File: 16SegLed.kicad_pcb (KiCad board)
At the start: 2 copper layers, 99.9 x 79.6 mm, 57 parts, among them J1 Conn_01x10, J2 Conn_01x10, J3 Conn_01x10, J4 Conn_01x06_Socket, J5 Conn_01x04_Pin, J6 Conn_01x04_Pin, Q1 BSS138, Q2 BSS138, SW1 SW_Push, SW2 SW_Push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

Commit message: Use meaningful segment net names
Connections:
- net /DisplayGroup0/SEG0 renamed /DisplayGroup0/SEG_{E}
- net /DisplayGroup0/SEG1 renamed /DisplayGroup0/SEG_{N}
- net /DisplayGroup0/SEG10 renamed /DisplayGroup0/SEG_{G1}
- net /DisplayGroup0/SEG11 renamed /DisplayGroup0/SEG_{K}
- net /DisplayGroup0/SEG12 renamed /DisplayGroup0/SEG_{J}
- net /DisplayGroup0/SEG13 renamed /DisplayGroup0/SEG_{H}
- net /DisplayGroup0/SEG14 renamed /DisplayGroup0/SEG_{F}
- net /DisplayGroup0/SEG2 renamed /DisplayGroup0/SEG_{M}
- net /DisplayGroup0/SEG3 renamed /DisplayGroup0/SEG_{L}
- net /DisplayGroup0/SEG4 renamed /DisplayGroup0/SEG_{G2}
- net /DisplayGroup0/SEG5 renamed /DisplayGroup0/SEG_{D}
- net /DisplayGroup0/SEG6 renamed /DisplayGroup0/SEG_{dp}
- net /DisplayGroup0/SEG7 renamed /DisplayGroup0/SEG_{C}
- net /DisplayGroup0/SEG8 renamed /DisplayGroup0/SEG_{B}
- net /DisplayGroup0/SEG9 renamed /DisplayGroup0/SEG_{A}
- net /DisplayGroup1/SEG0 renamed /DisplayGroup1/SEG_{E}
- net /DisplayGroup1/SEG1 renamed /DisplayGroup1/SEG_{N}
- net /DisplayGroup1/SEG10 renamed /DisplayGroup1/SEG_{G1}
- net /DisplayGroup1/SEG11 renamed /DisplayGroup1/SEG_{K}
- net /DisplayGroup1/SEG12 renamed /DisplayGroup1/SEG_{J}
- net /DisplayGroup1/SEG13 renamed /DisplayGroup1/SEG_{H}
- net /DisplayGroup1/SEG14 renamed /DisplayGroup1/SEG_{F}
- net /DisplayGroup1/SEG2 renamed /DisplayGroup1/SEG_{M}
- net /DisplayGroup1/SEG3 renamed /DisplayGroup1/SEG_{L}
- net /DisplayGroup1/SEG4 renamed /DisplayGroup1/SEG_{G2}
- net /DisplayGroup1/SEG5 renamed /DisplayGroup1/SEG_{D}
- net /DisplayGroup1/SEG6 renamed /DisplayGroup1/SEG_{dp}
- net /DisplayGroup1/SEG7 renamed /DisplayGroup1/SEG_{C}
- net /DisplayGroup1/SEG8 renamed /DisplayGroup1/SEG_{B}
- net /DisplayGroup1/SEG9 renamed /DisplayGroup1/SEG_{A}

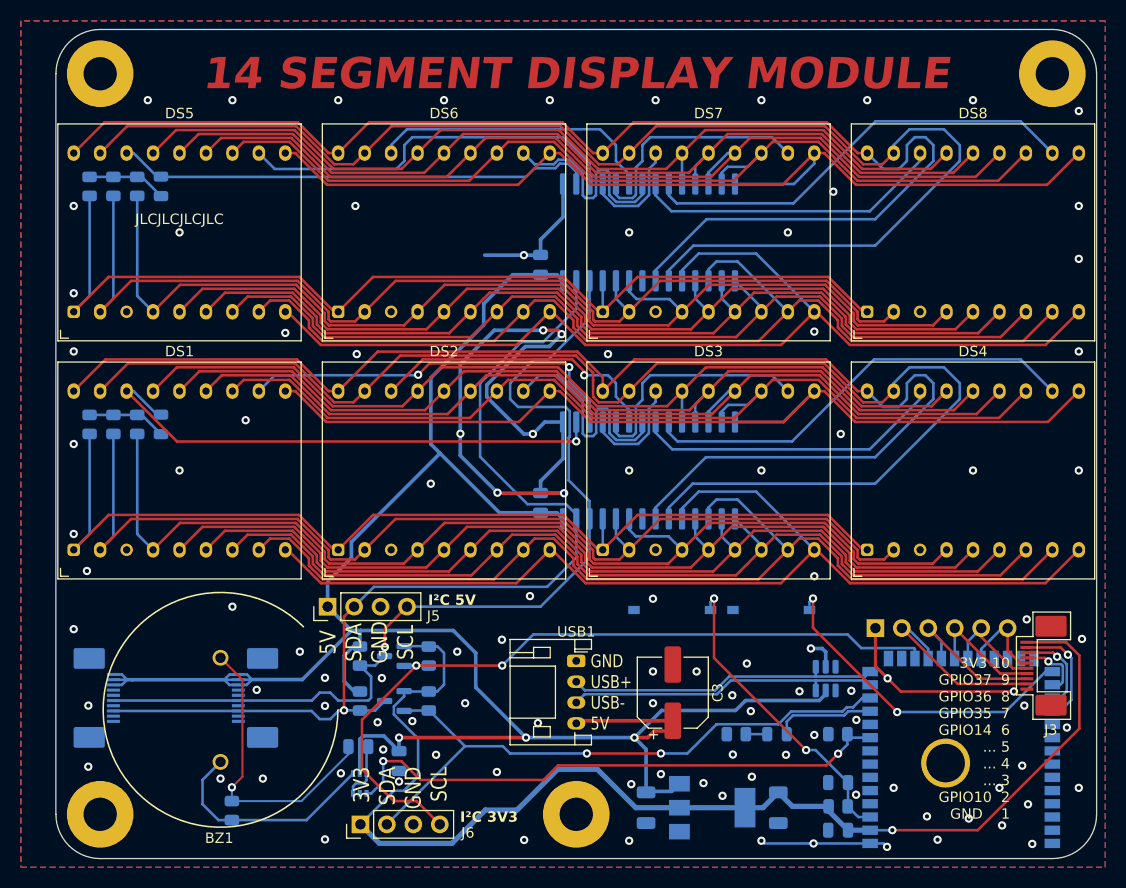
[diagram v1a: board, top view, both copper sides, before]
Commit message: Rearrange ROW assignment so digits are scanned consecutively from left to right
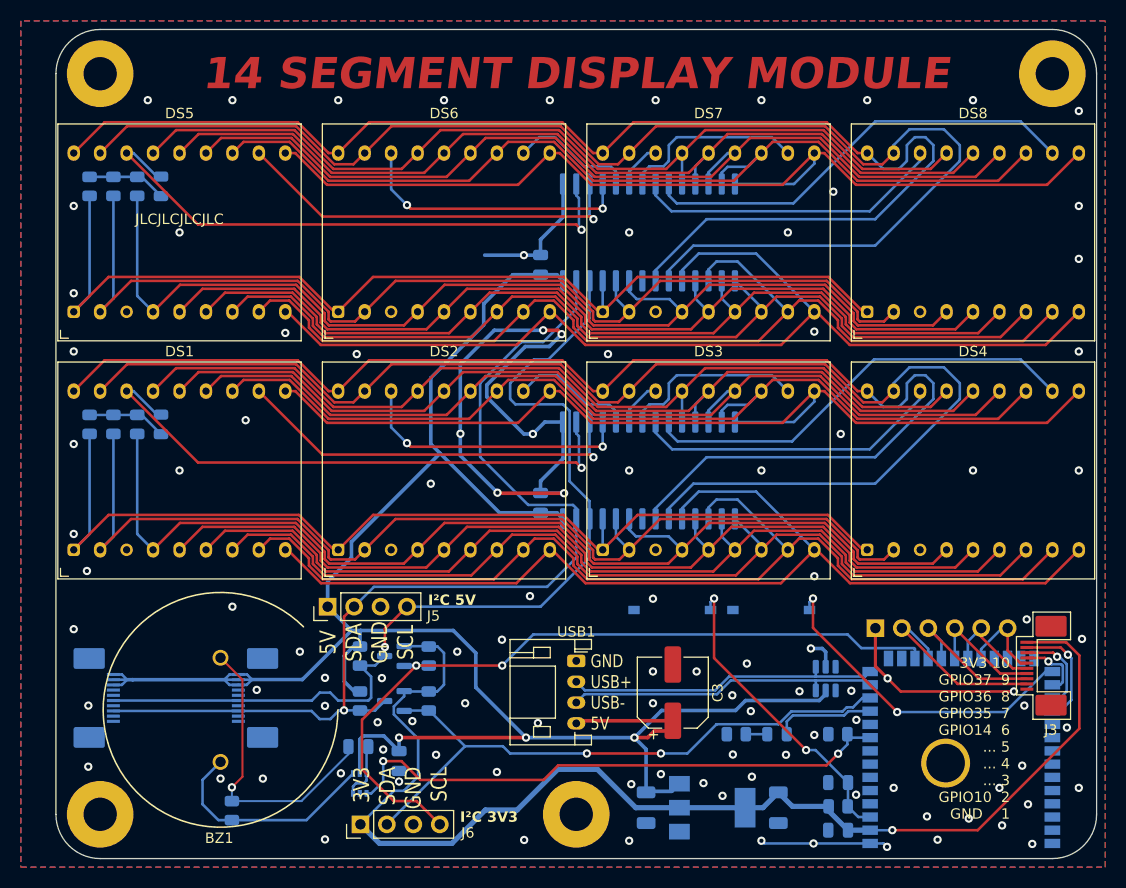
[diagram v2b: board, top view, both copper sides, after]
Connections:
- DS2 pad 11: /DisplayGroup0/COM5 -> /DisplayGroup0/COM3
- DS2 pad 16: /DisplayGroup0/COM4 -> /DisplayGroup0/COM2
- DS3 pad 11: /DisplayGroup0/COM3 -> /DisplayGroup0/COM5
- DS3 pad 16: /DisplayGroup0/COM2 -> /DisplayGroup0/COM4
- DS6 pad 11: /DisplayGroup1/COM5 -> /DisplayGroup1/COM3
- DS6 pad 16: /DisplayGroup1/COM4 -> /DisplayGroup1/COM2
- DS7 pad 11: /DisplayGroup1/COM3 -> /DisplayGroup1/COM5
- DS7 pad 16: /DisplayGroup1/COM2 -> /DisplayGroup1/COM4
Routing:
- net /DisplayGroup0/COM4: track 28.3 -> 4.47 mm, vias 1 -> 0
- net /DisplayGroup1/COM4: track 27.9 -> 4.47 mm
- net /DisplayGroup0/COM2: track 10.6 -> 26.9 mm, vias 0 -> 2
- net /DisplayGroup1/COM2: track 10.6 -> 26.9 mm, vias 0 -> 2
- net /DisplayGroup0/COM3: track 23.2 -> 12.0 mm
- net /DisplayGroup1/COM3: track 23.2 -> 12.1 mm
- net /DisplayGroup1/COM0: track 46.1 -> 55.6 mm, vias 0 -> 1
- net /DisplayGroup0/COM5: track 22.5 -> 18.0 mm
- net /DisplayGroup0/COM0: track 51.3 -> 55.6 mm
- net /DisplayGroup1/COM5: track 21.0 -> 18.0 mm
- net /DisplayGroup0/SEG_{H}: track 130.7 -> 128.5 mm
- net /DisplayGroup0/SEG_{F}: track 128.2 -> 126.6 mm
- net /DisplayGroup0/COM1: track 37.1 -> 38.3 mm, vias 2 -> 1
- net /DisplayGroup0/SEG_{B}: track 92.4 -> 93.2 mm
- net /DisplayGroup1/COM1: track 37.5 -> 38.3 mm, vias 0 -> 1
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
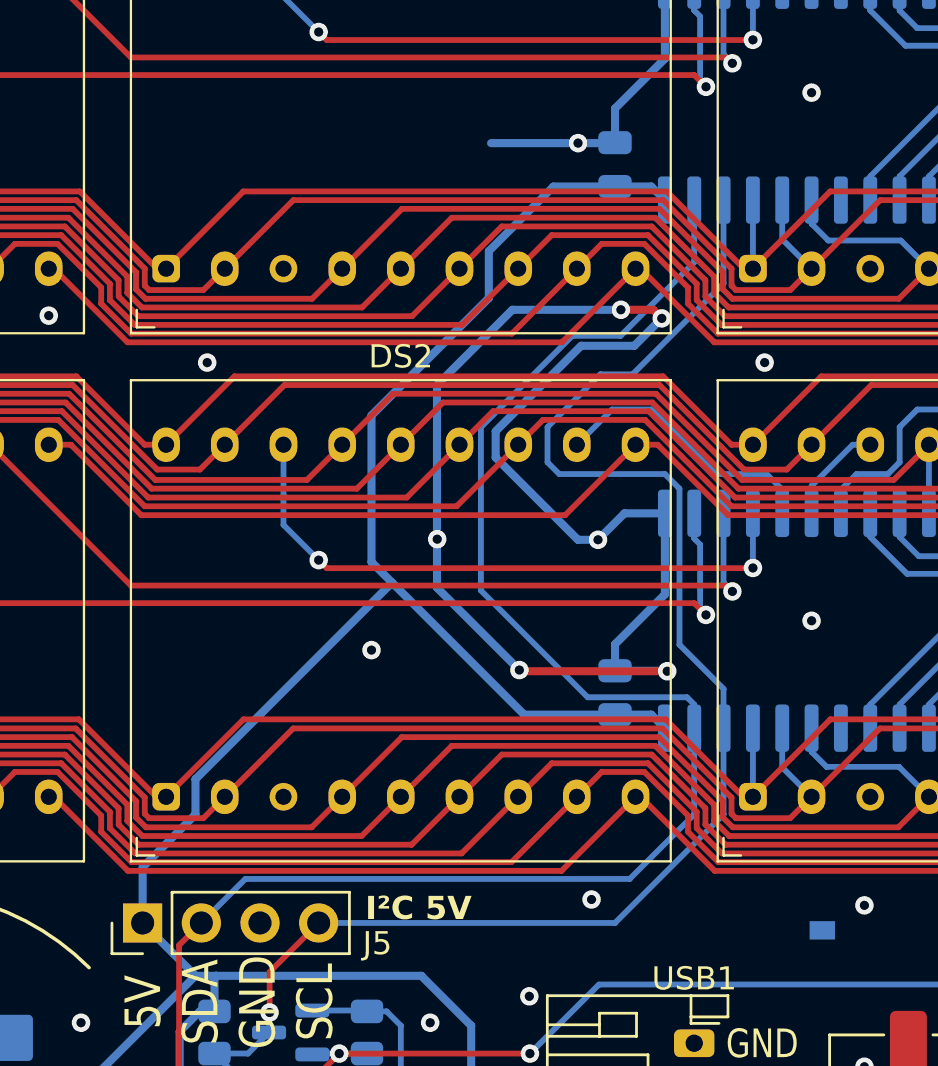
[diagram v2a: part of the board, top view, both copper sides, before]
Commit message: Improve routing of power and I2C nets for LED drivers
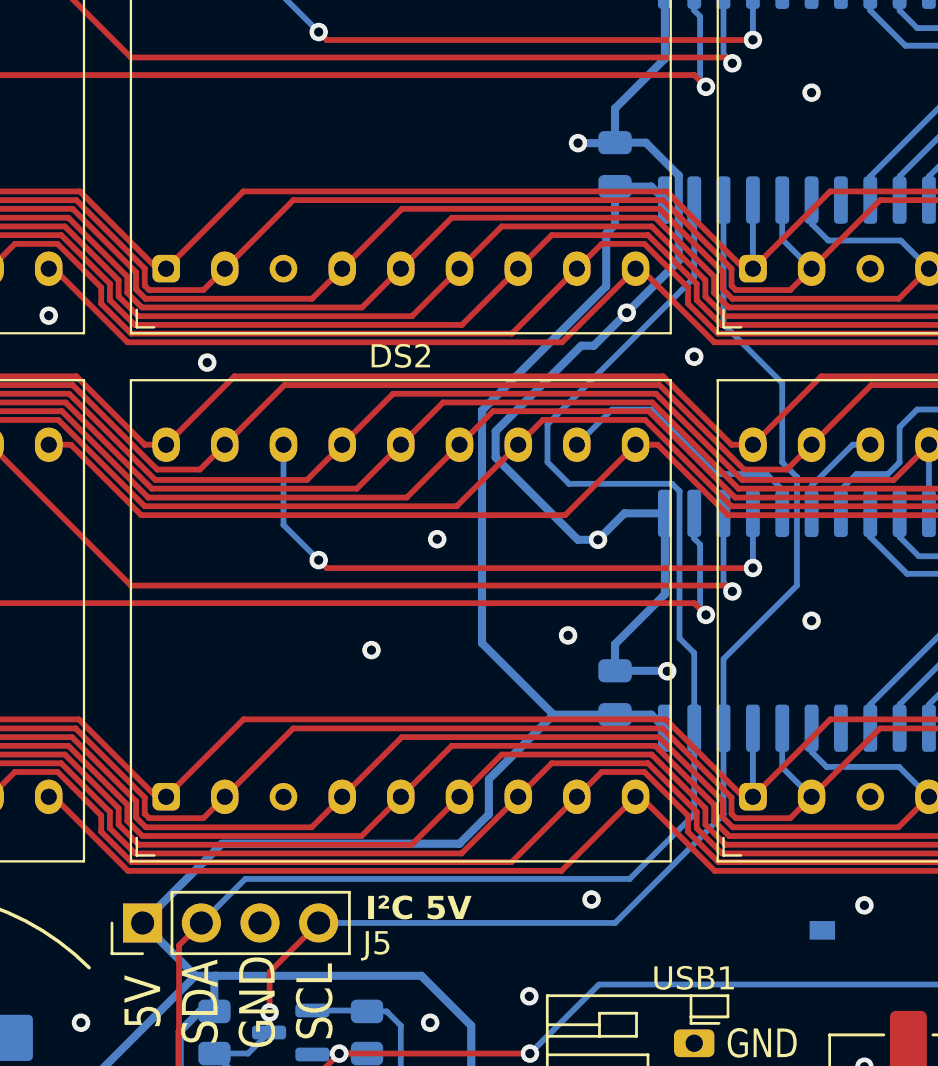
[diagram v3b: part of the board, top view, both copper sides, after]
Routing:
- net GND: track 107.6 -> 81.2 mm, vias 108 -> 107
- net /SCL5V: track 93.3 -> 86.1 mm
- net /SDA5V: track 98.7 -> 95.2 mm
- net +5V: track 203.1 -> 200.0 mm
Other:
- board text added: "2024-JAN-07"
- board text removed: "2024-JAN-06"

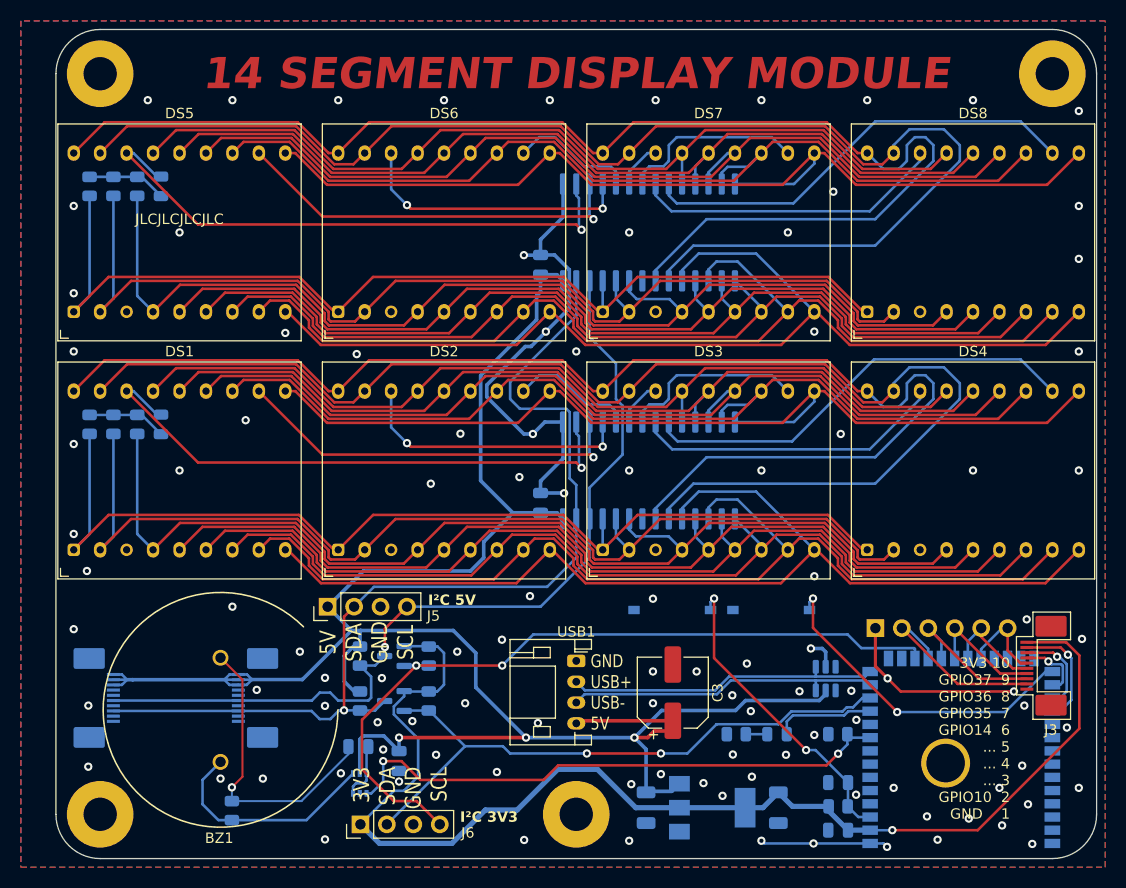
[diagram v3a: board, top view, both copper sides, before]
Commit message: Rearrange GND vias
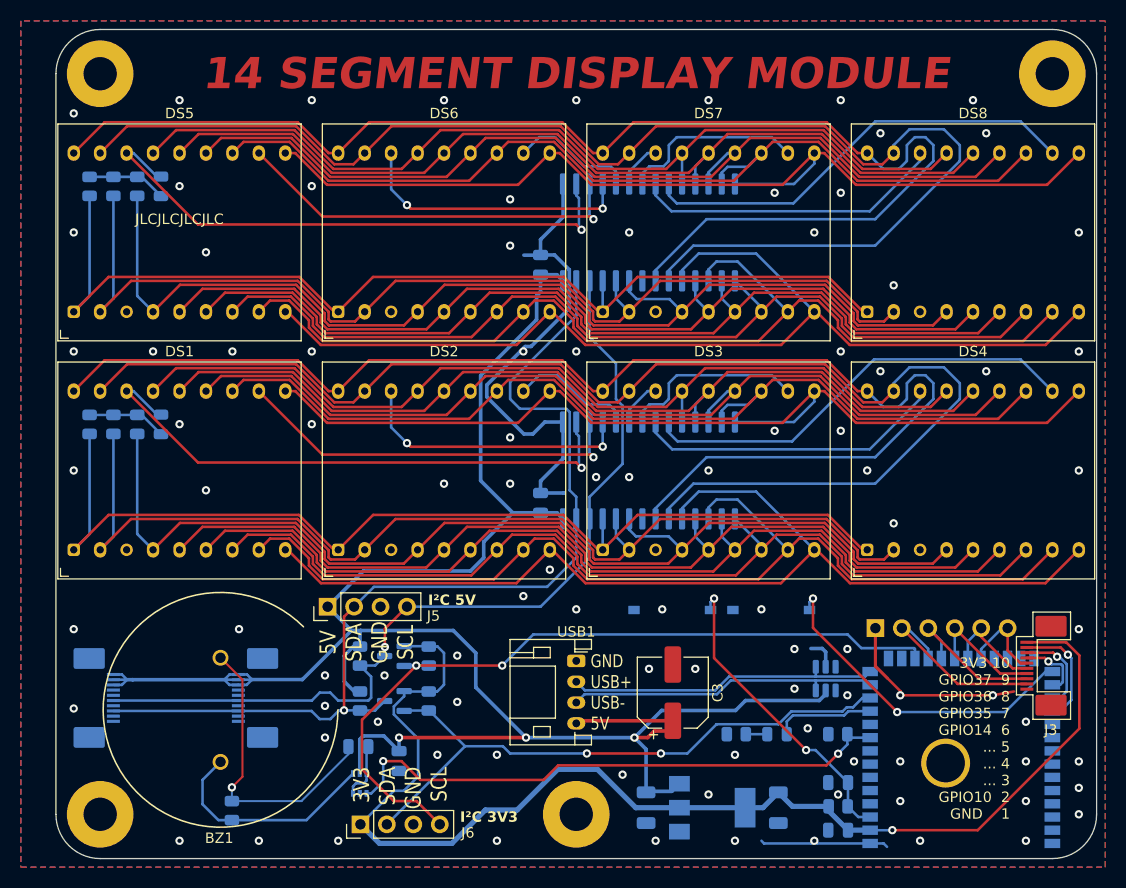
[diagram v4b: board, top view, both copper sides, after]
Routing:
- net GND: track 81.2 -> 81.8 mm, vias 107 -> 96

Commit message: Connect mounting holes to ground
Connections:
- H1 pad 1: (no net) -> GND
- H2 pad 1: (no net) -> GND
- H3 pad 1: (no net) -> GND
- H4 pad 1: (no net) -> GND
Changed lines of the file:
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@@
     (property "Sheetfile" "16SegLed.kicad_sch")
     (property "Sheetname" "")
-    (property "dnp" "")
-    (property "exclude_from_bom" "")
-    (property "ki_description" "Mounting Hole without connection")
+    (property "ki_description" "Mounting Hole with connection")
     (property "ki_keywords" "mounting hole")
-    (attr exclude_from_pos_files exclude_from_bom)
+    (attr exclude_from_pos_files)
     (fp_text reference "H2" (at 0 -4.2) (layer "F.SilkS") hide
         (effects (font (size 1 1) (thickness 0.15)))
@@
         (effects (font (size 1 1) (thickness 0.15)))
     )
+    (fp_text user "${REFERENCE}" (at 0 0) (layer "F.Fab")
+        (effects (font (size 1 1) (thickness 0.15)))
+    )
     (fp_circle (center 0 0) (end 3.2 0)
       (stroke (width 0.15) (type solid)) (fill none) (layer "Cmts.User"))
     (fp_circle (center 0 0) (end 3.45 0)
       (stroke (width 0.05) (type solid)) (fill none) (layer "F.CrtYd"))
-    (pad "1" thru_hole circle (at 0 0) (size 6.4 6.4) (drill 3.2) (layers "*.Cu" "*.Mask"))
+    (pad "1" thru_hole circle (at 0 0) (size 6.4 6.4) (drill 3.2) (layers "*.Cu" "*.Mask")
+      (net 5 "GND") (pinfunction "1") (pintype "input"))
   )
   (footprint "Connector_JST:JST_PH_S4B-PH-K_1x04_P2.00mm_Horizontal" (layer "F.Cu")
@@
     (property "Sheetfile" "16SegLed.kicad_sch")
     (property "Sheetname" "")
-    (property "dnp" "")
-    (property "exclude_from_bom" "")
-    (property "ki_description" "Mounting Hole without connection")
+    (property "ki_description" "Mounting Hole with connection")
     (property "ki_keywords" "mounting hole")
-    (attr exclude_from_pos_files exclude_from_bom)
+    (attr exclude_from_pos_files)
     (fp_text reference "H1" (at 0 -4.2) (layer "F.SilkS") hide
         (effects (font (size 1 1) (thickness 0.15)))
@@
         (effects (font (size 1 1) (thickness 0.15)))
     )
+    (fp_text user "${REFERENCE}" (at 0 0) (layer "F.Fab")
+        (effects (font (size 1 1) (thickness 0.15)))
+    )
     (fp_circle (center 0 0) (end 3.2 0)
       (stroke (width 0.15) (type solid)) (fill none) (layer "Cmts.User"))
     (fp_circle (center 0 0) (end 3.45 0)
       (stroke (width 0.05) (type solid)) (fill none) (layer "F.CrtYd"))
-    (pad "1" thru_hole circle (at 0 0) (size 6.4 6.4) (drill 3.2) (layers "*.Cu" "*.Mask"))
+    (pad "1" thru_hole circle (at 0 0) (size 6.4 6.4) (drill 3.2) (layers "*.Cu" "*.Mask")
+      (net 5 "GND") (pinfunction "1") (pintype "input"))
   )
   (footprint "ProjectLibrary:DIP-18_600_ELL" (layer "F.Cu")
@@
     (property "Sheetfile" "16SegLed.kicad_sch")
     (property "Sheetname" "")
-    (property "dnp" "")
-    (property "exclude_from_bom" "")
-    (property "ki_description" "Mounting Hole without connection")
+    (property "ki_description" "Mounting Hole with connection")
     (property "ki_keywords" "mounting hole")
-    (attr exclude_from_pos_files exclude_from_bom)
+    (attr exclude_from_pos_files)
     (fp_text reference "H4" (at 0 4.2) (layer "B.SilkS") hide
         (effects (font (size 1 1) (thickness 0.15)) (justify mirror))
@@
     (fp_circle (center 0 0) (end 3.45 0)
       (stroke (width 0.05) (type solid)) (fill none) (layer "B.CrtYd"))
-    (pad "1" thru_hole circle (at 0 0 180) (size 6.4 6.4) (drill 3.2) (layers "*.Cu" "*.Mask"))
+    (pad "1" thru_hole circle (at 0 0 180) (size 6.4 6.4) (drill 3.2) (layers "*.Cu" "*.Mask")
+      (net 5 "GND") (pinfunction "1") (pintype "input"))
   )
   (footprint "Capacitor_SMD:C_0805_2012Metric" (layer "B.Cu")
@@
     (property "Sheetfile" "16SegLed.kicad_sch")
     (property "Sheetname" "")
-    (property "dnp" "")
-    (property "exclude_from_bom" "")
-    (property "ki_description" "Mounting Hole without connection")
+    (property "ki_description" "Mounting Hole with connection")
     (property "ki_keywords" "mounting hole")
-    (attr exclude_from_pos_files exclude_from_bom)
+    (attr exclude_from_pos_files)
     (fp_text reference "H3" (at 0 4.2) (layer "B.SilkS") hide
         (effects (font (size 1 1) (thickness 0.15)) (justify mirror))
@@
         (effects (font (size 1 1) (thickness 0.15)) (justify mirror))
     )
+    (fp_text user "${REFERENCE}" (at 0 0) (layer "B.Fab")
+        (effects (font (size 1 1) (thickness 0.15)) (justify mirror))
+    )
     (fp_circle (center 0 0) (end 3.2 0)
       (stroke (width 0.15) (type solid)) (fill none) (layer "Cmts.User"))
     (fp_circle (center 0 0) (end 3.45 0)
       (stroke (width 0.05) (type solid)) (fill none) (layer "B.CrtYd"))
-    (pad "1" thru_hole circle (at 0 0 180) (size 6.4 6.4) (drill 3.2) (layers "*.Cu" "*.Mask"))
+    (pad "1" thru_hole circle (at 0 0 180) (size 6.4 6.4) (drill 3.2) (layers "*.Cu" "*.Mask")
+      (net 5 "GND") (pinfunction "1") (pintype "input"))
   )
   (footprint "Resistor_SMD:R_0805_2012Metric" (layer "B.Cu")
